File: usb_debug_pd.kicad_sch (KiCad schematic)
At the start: 85 parts, among them J7 Tag-Connect_TC2050-IDC-NL_2x5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, J8 USB-C_GCT_USB4105-GF-A, Q12 PJE138K, Q20 PJE138K, U29 W25Q80DV_USON, U30 TPS65988DHRSHR, U31 NTS0102_XSON, U32 NCP730BMT330_WSON, U34 FT230X_QFN, U40 AP22615A_TSOT26, U42 TPD4E05U06QDQARQ1

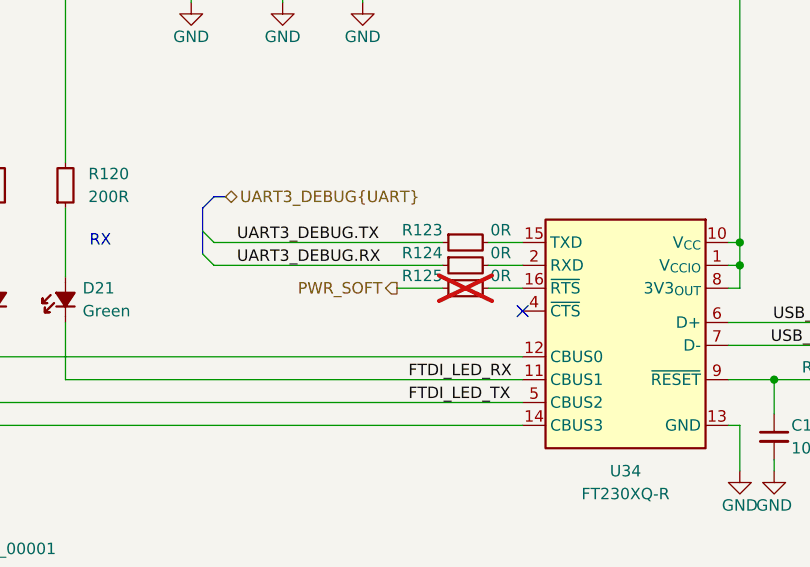
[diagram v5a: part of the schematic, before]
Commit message: [#82837] Finish Power-up and reset section
[#82837] Add 1V8 buck converter and wire power seqencer programmer

[#82837] WIP: Add 18V DC-DC converter

[#82837] Ditch idea of 18V DC-DC converter, for seqencing just use power mosfets to supply High voltage to SOM, modify VCC line for higher voltage
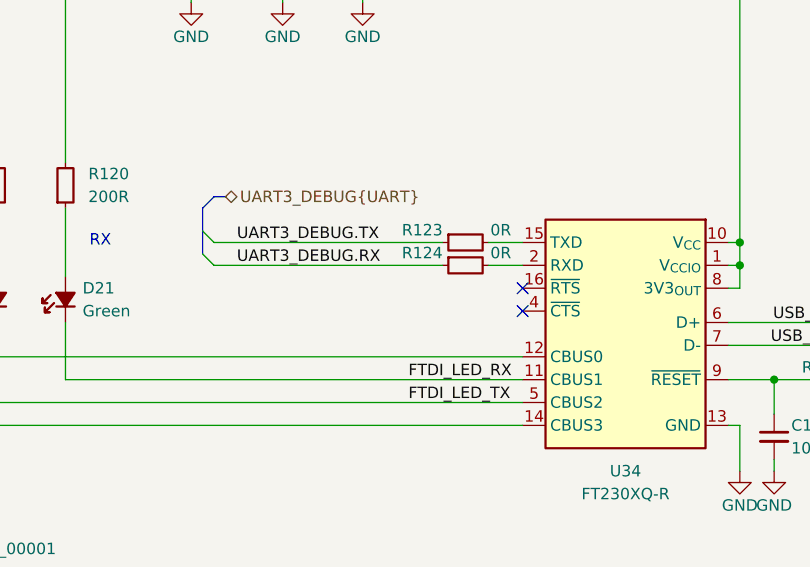
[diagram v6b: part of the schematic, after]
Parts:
- removed R125: R_0R_0402, antmicro-footprints:R_0402_1005Metric, symbol antmicroResistors0402:R_0R_0402
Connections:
- no-connect marks 14 -> 15
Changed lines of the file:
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@@
 	)
 	(no_connect
+		(at 171.45 104.14)
+	)
+	(no_connect
 		(at 231.14 190.5)
 	)
@@
 	(wire
 		(pts
-			(xy 162.56 104.14) (xy 157.48 104.14)
-		)
-		(stroke
-			(width 0)
-			(type default)
-		)
-	)
-	(wire
-		(pts
 			(xy 261.62 247.65) (xy 280.67 247.65)
 		)
@@
 	(wire
 		(pts
-			(xy 171.45 104.14) (xy 167.64 104.14)
-		)
-		(stroke
-			(width 0)
-			(type default)
-		)
-	)
-	(wire
-		(pts
 			(xy 50.8 119.38) (xy 50.8 120.65)
 		)
@@
 		)
 	)
-	(hierarchical_label "PWR_SOFT"
-		(shape output)
-		(at 157.48 104.14 180)
-		(effects
-			(font
-				(size 1.27 1.27)
-			)
-			(justify right)
-		)
-	)
 	(hierarchical_label "~{PDC_I2C1_IRQ}"
 		(shape input)
@@
 					(unit 1)
 				)
-			)
-		)
-	)
-	(symbol
-		(lib_name "R_0R_0402_6")
-		(lib_id "antmicroResistors0402:R_0R_0402")
-		(at 162.56 104.14 0)
-		(unit 1)
-		(exclude_from_sim no)
-		(in_bom no)
-		(on_board yes)
-		(dnp yes)
-		(property "Reference" "R125"
-			(at 162.56 103.505 0)
-			(effects
-				(font
-					(size 1.27 1.27)
-				)
-				(justify right bottom)
-			)
-		)
-		(property "Value" "R_0R_0402"
-			(at 182.88 116.84 0)
-			(effects
-				(font
-					(size 1.27 1.27)
-					(thickness 0.15)
-				)
-				(justify left bottom)
-				(hide yes)
-			)
-		)
-		(property "Footprint" "antmicro-footprints:R_0402_1005Metric"
-			(at 182.88 119.38 0)
-			(effects
-				(font
-					(size 1.27 1.27)
-					(thickness 0.15)
-				)
-				(justify left bottom)
-				(hide yes)
-			)
-		)
-		(property "Datasheet" "https://industrial.panasonic.com/cdbs/www-data/pdf/RDA0000/AOA0000C301.pdf"
-			(at 182.88 121.92 0)
-			(effects
-				(font
-					(size 1.27 1.27)
-					(thickness 0.15)
-				)
-				(justify left bottom)
-				(hide yes)
-			)
-		)
-		(property "Description" ""
-			(at 162.56 104.14 0)
-			(effects
-				(font
-					(size 1.27 1.27)
-				)
-				(hide yes)
-			)
-		)
-		(property "Manufacturer" "Panasonic"
-			(at 182.88 127 0)
-			(effects
-				(font
-					(size 1.27 1.27)
-					(thickness 0.15)
-				)
-				(justify left bottom)
-				(hide yes)
-			)
-		)
-		(property "MPN" "ERJ2GE0R00X"
-			(at 182.88 124.46 0)
-			(effects
-				(font
-					(size 1.27 1.27)
-					(thickness 0.15)
-				)
-				(justify left bottom)
-				(hide yes)
-			)
-		)
-		(property "Val" "0R"
-			(at 170.18 103.505 0)
-			(effects
-				(font
-					(size 1.27 1.27)
-					(thickness 0.15)
-				)
-				(justify right bottom)
-			)
-		)
-		(property "License" "Apache-2.0"
-			(at 182.88 129.54 0)
-			(effects
-				(font
-					(size 1.27 1.27)
-					(thickness 0.15)
-				)
-				(justify left bottom)
-				(hide yes)
-			)
-		)
-		(property "Author" "Antmicro"
-			(at 182.88 132.08 0)
-			(effects
-				(font
-					(size 1.27 1.27)
-					(thickness 0.15)
-				)
-				(justify left bottom)
-				(hide yes)
-			)
-		)
-		(property "Tolerance" "~"
-			(at 182.88 114.3 0)
-			(effects
-				(font
-					(size 1.27 1.27)
-				)
-				(justify left bottom)
-				(hide yes)
-			)
-		)
-		(property "Current" "1A"
-			(at 182.88 134.62 0)
-			(effects
-				(font
-					(size 1.27 1.27)
-					(thickness 0.15)
-				)
-				(justify left bottom)
-				(hide yes)
-			)
-		)
-		(pin "1"
-		)
-		(pin "2"
-		)
-		(instances
-			(project "jetson-agx-thor-baseboard"
-				(path "/f569b0be-0afd-48b7-93ee-28582a4c645c/12c19ba5-8fdc-4775-a33b-e8b1ade01b0a"
-					(reference "R125")
-					(unit 1)
-				)

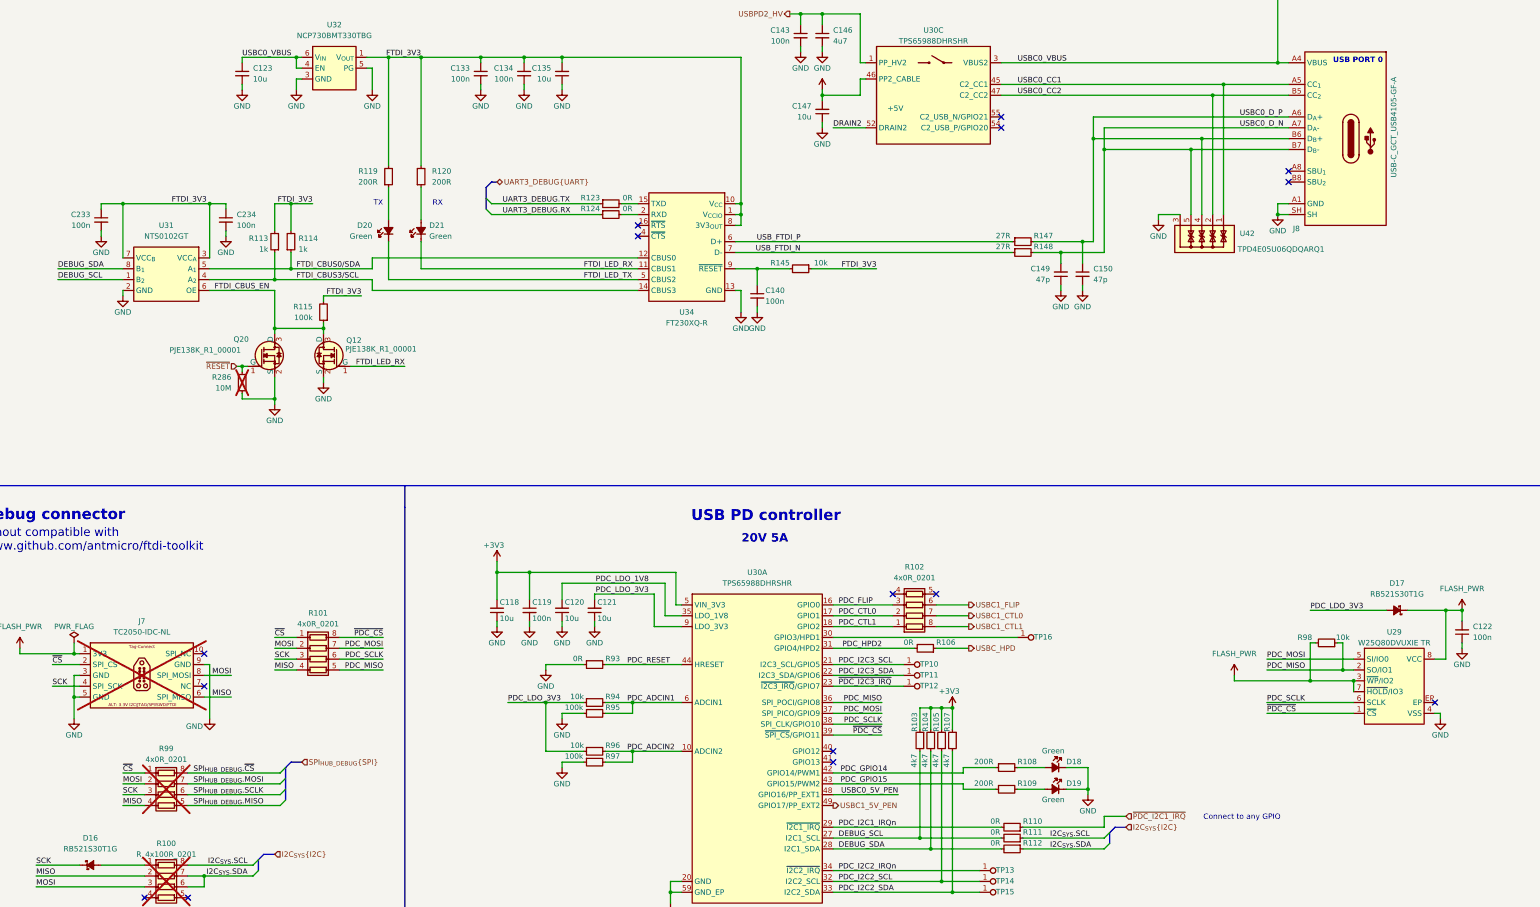
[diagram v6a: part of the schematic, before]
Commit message: [#82837] Finish mapping PCIe and SFP+ connections on SoM
[#82837] WIP: correct ERC errors

[#82837] WIP: correct ERC errors, fix signal direction of most buses

[#82837] Fix all ERC errors
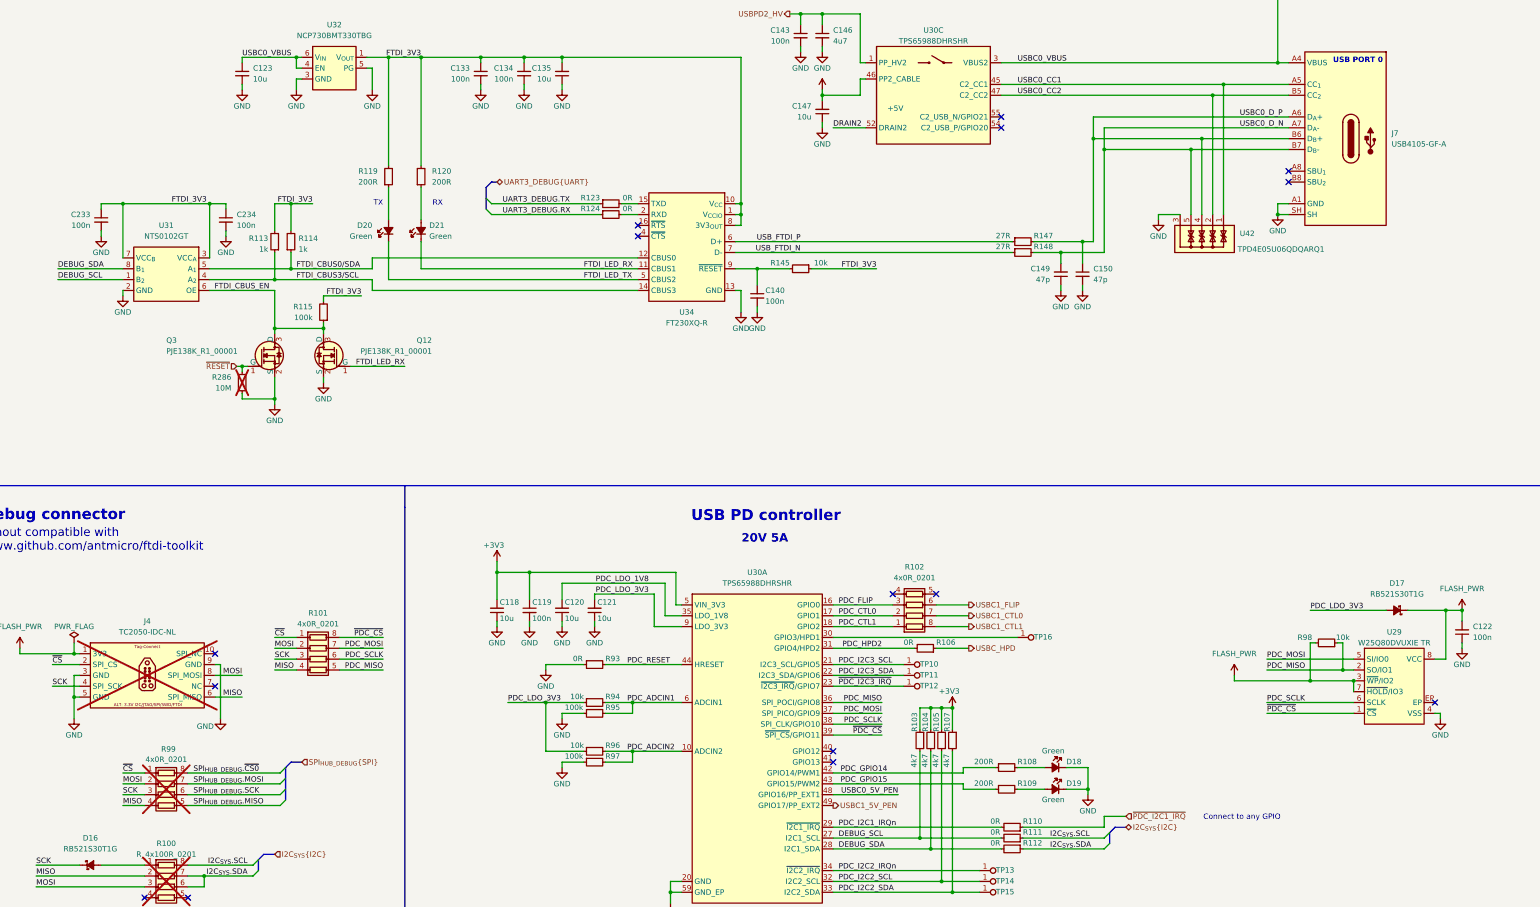
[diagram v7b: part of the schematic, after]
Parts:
- removed J7: Tag-Connect_TC2050-IDC-NL_2x5_P1.27mm, antmicro-footprints:Tag-Connect_TC2050-IDC-NL_2x5_P1.27mm, symbol antmicroTestPoints:Tag-Connect_TC2050-IDC-NL_2x5_P1.27mm
- removed J8: USB-C_GCT_USB4105-GF-A, antmicro-footprints:USB-C_Receptacle_GCT_USB4105-GF-A, symbol antmicroUSBConnectors:USB-C_GCT_USB4105-GF-A
- removed Q20: PJE138K, antmicro-footprints:SOT-523, symbol antmicroTransistorsFETsMOSFETsSingle:PJE138K
- added J4: Tag-Connect_TC2050-IDC-NL_2x5_P1.27mm, antmicro-footprints:Tag-Connect_TC2050-IDC-NL_2x5_P1.27mm, symbol antmicroTestPoints:Tag-Connect_TC2050-IDC-NL_2x5_P1.27mm
- added J7: USB-C_GCT_USB4105-GF-A, antmicro-footprints:USB-C_Receptacle_GCT_USB4105-GF-A, symbol antmicroUSBConnectors:USB-C_GCT_USB4105-GF-A
- added Q3: PJE138K, antmicro-footprints:SOT-523, symbol antmicroTransistorsFETsMOSFETsSingle:PJE138K
- Q12: now left out of the parts list
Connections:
- net FLASH_PWR: now also J4.1
- net FTDI_CBUS_EN: now also Q3.3 (D)
- net GND: now also J4.3, J4.5, J4.9, J7.A1 (GND), J7.A12 (GND), J7.B1 (GND), J7.B12 (GND), J7.SH, Q3.2 (S)
- net MISO: now also J4.6
- net MOSI: now also J4.8
- net SCK: now also J4.4
- net USBC0_CC1: now also J7.A5 (CC_{1})
- net USBC0_CC2: now also J7.B5 (CC_{2})
- net USBC0_D_N: now also J7.A7 (D_{A}-), J7.B7 (D_{B}-)
- net USBC0_D_P: now also J7.A6 (D_{A}+), J7.B6 (D_{B}+)
- net USBC0_VBUS: now also J7.A4 (VBUS), J7.A9 (VBUS), J7.B4 (VBUS), J7.B9 (VBUS)
- net ~{CS}: now also J4.2
- net ~{RESET}: now also Q3.1 (G)
- net SPI_{HUB_DEBUG}.SCLK renamed SPI_{HUB_DEBUG}.SCK
- net SPI_{HUB_DEBUG}.~{CS} renamed SPI_{HUB_DEBUG}.~{CS0}
